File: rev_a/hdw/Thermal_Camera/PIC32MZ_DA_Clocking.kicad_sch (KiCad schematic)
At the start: 17 parts, among them U1101 74LVC1G97, X1101 ASE-8.000MHz, X1102 ECS-327KE

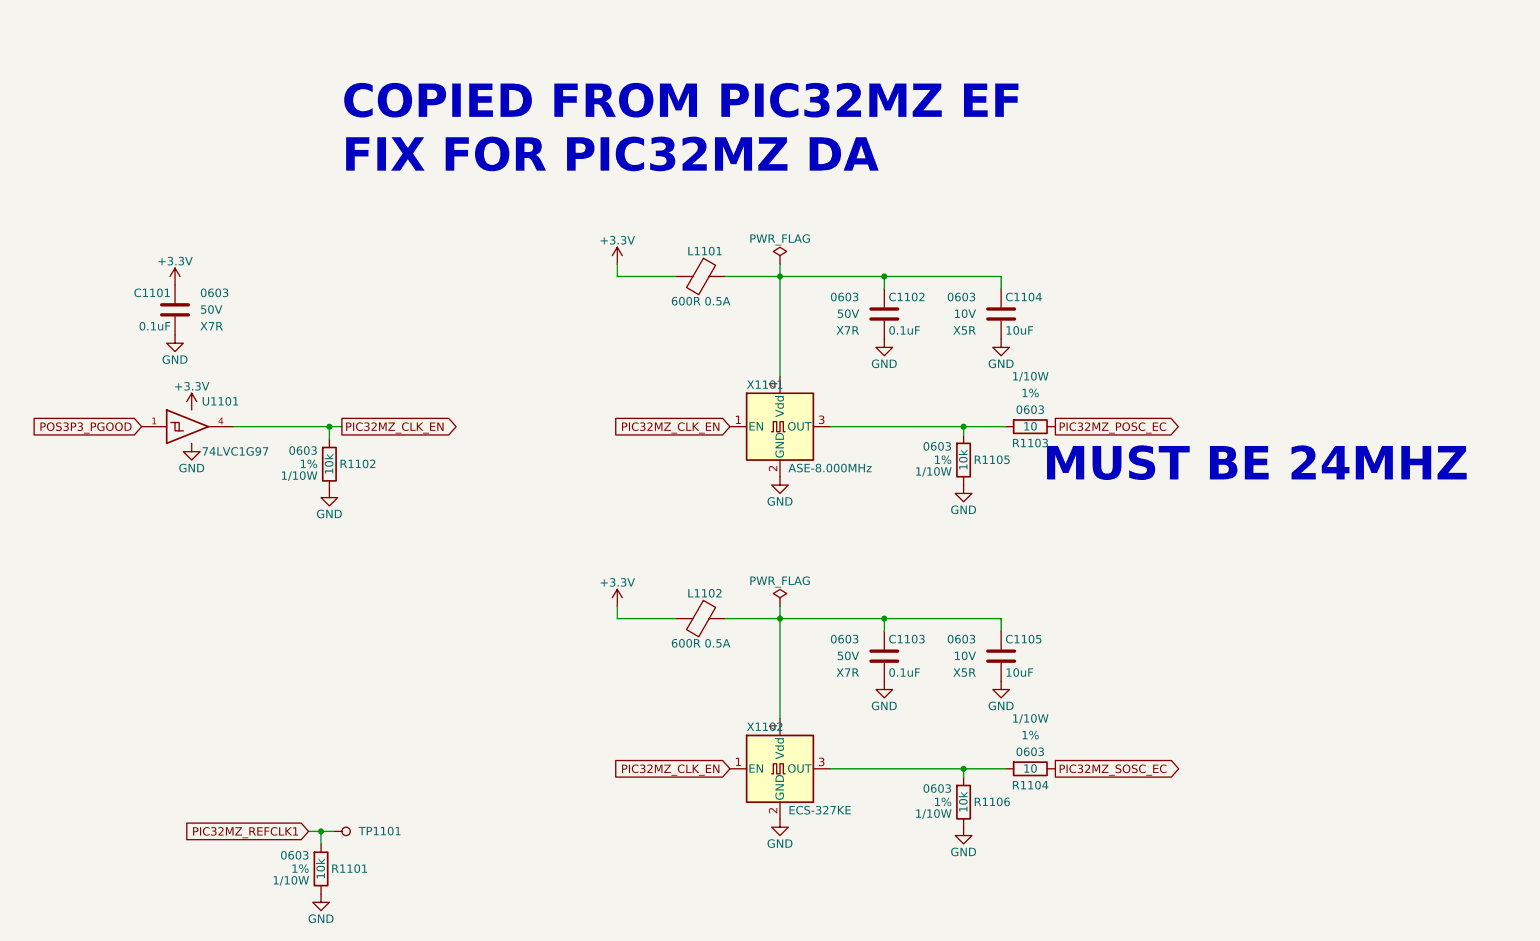
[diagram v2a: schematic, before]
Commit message: changed a lot of circuits from +3.3V to +3.0V VDD
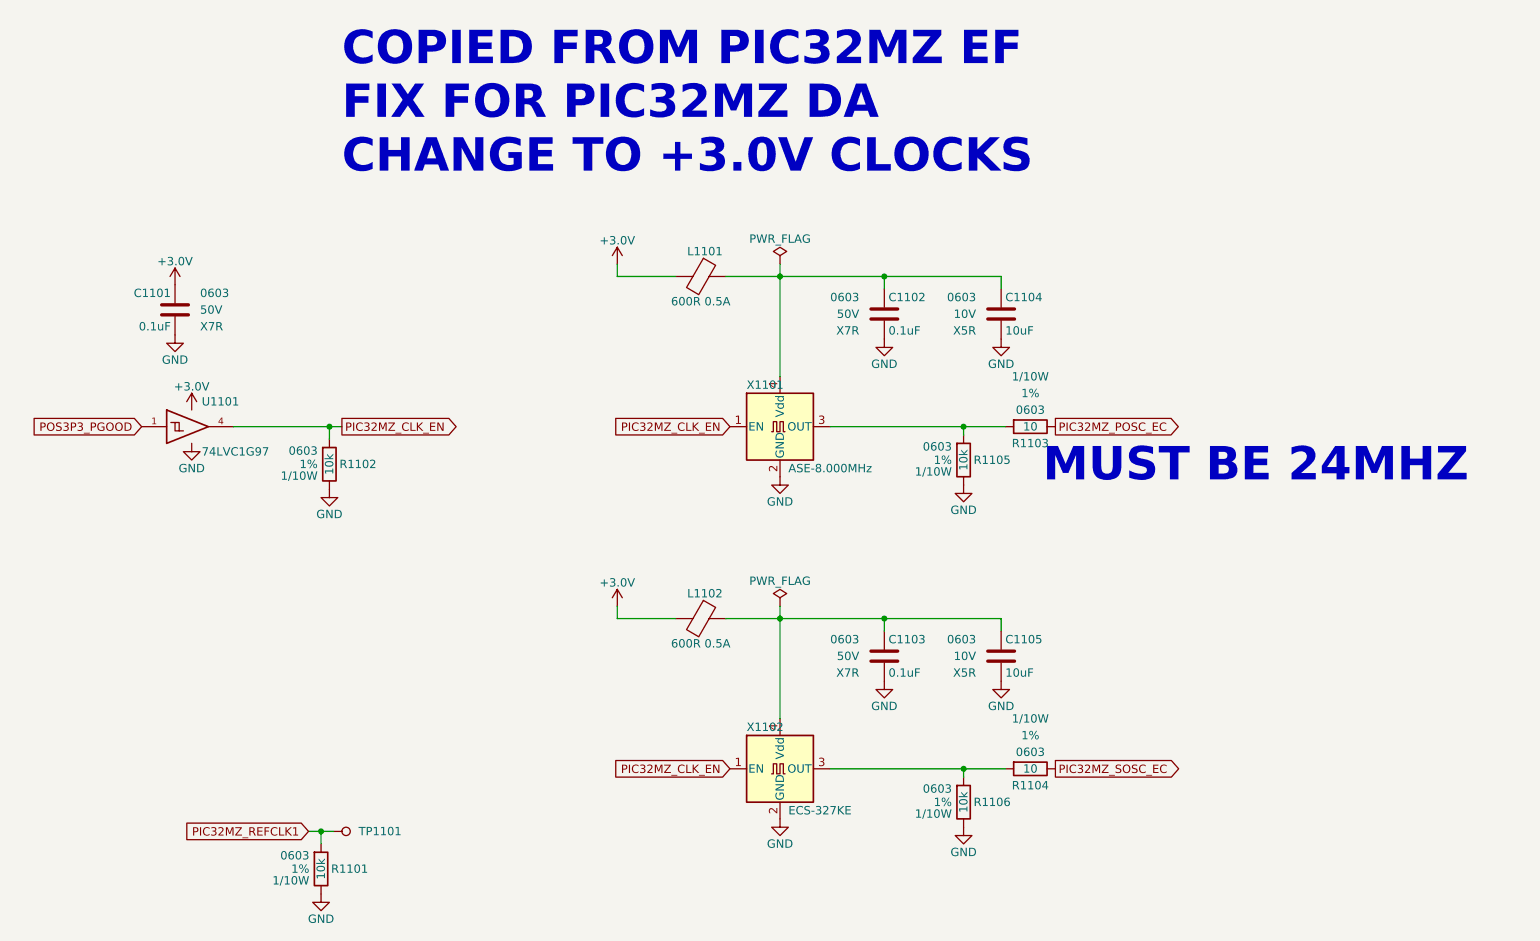
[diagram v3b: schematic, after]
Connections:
- net +3.3V renamed +3.0V
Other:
- note added: "COPIED FROM PIC32MZ EF FIX FOR PIC32MZ DA CHANGE TO +3.0V CLOCKS"
- note removed: "COPIED FROM PIC32MZ EF FIX FOR PIC32MZ DA"
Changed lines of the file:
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@@
     (effects (font (size 5.08 5.08) (thickness 1.016) bold (color 194 0 0 1)) (justify left bottom))
   )
-  (text "COPIED FROM PIC32MZ EF\nFIX FOR PIC32MZ DA" (at 86.36 35.56 0)
+  (text "COPIED FROM PIC32MZ EF\nFIX FOR PIC32MZ DA\nCHANGE TO +3.0V CLOCKS"
+    (at 86.36 35.56 0)
     (effects (font (size 5.08 5.08) (thickness 1.016) bold (color 194 0 0 1)) (justify left bottom))
   )
@@
     )
   )
-  (symbol (lib_id "power:+3.3V") (at 128.27 48.895 0) (unit 1)
-    (in_bom yes) (on_board yes) (dnp no)
-    (property "Reference" "#PWR01107" (at 128.27 52.705 0)
-      (effects (font (size 1.27 1.27)) hide)
-    )
-    (property "Value" "+3.3V" (at 128.27 45.339 0)
-      (effects (font (size 1.27 1.27)))
-    )
-    (property "Footprint" "" (at 128.27 48.895 0)
-      (effects (font (size 1.27 1.27)) hide)
-    )
-    (property "Datasheet" "" (at 128.27 48.895 0)
-      (effects (font (size 1.27 1.27)) hide)
-    )
-    (pin "1")
-    (instances
-      (project "Nixie_Clock_Core"
-        (path "/16fdce21-b570-4d81-a458-e8839d611806/e5c9ef11-2d61-484d-80e2-ac34f2486528"
-          (reference "#PWR01107") (unit 1)
-        )
-      )
-      (project "LED_Panel_Controller"
-        (path "/22e05ee1-b227-4be7-9418-94433f274720/00000000-0000-0000-0000-00005f5829c2"
-          (reference "#PWR?") (unit 1)
-        )
-      )
-      (project "Thermal_Camera"
-        (path "/4bd21e0b-5408-4b93-866e-c82ac5b31fa9/b2bf3717-0f22-469b-940c-2d570066d2c6"
-          (reference "#PWR01007") (unit 1)
-        )
-      )
-    )
-  )
   (symbol (lib_id "Device:Ferrite_Bead") (at 140.97 50.8 270) (unit 1)
     (in_bom yes) (on_board yes) (dnp no)
@@
     )
   )
+  (symbol (lib_id "Custom Library:+3.0V") (at 128.27 100.965 0) (unit 1)
+    (in_bom yes) (on_board yes) (dnp no)
+    (property "Reference" "#PWR01651" (at 128.27 104.775 0)
+      (effects (font (size 1.27 1.27)) hide)
+    )
+    (property "Value" "+3.0V" (at 128.27 97.409 0)
+      (effects (font (size 1.27 1.27)))
+    )
+    (property "Footprint" "" (at 128.27 100.965 0)
+      (effects (font (size 1.27 1.27)) hide)
+    )
+    (property "Datasheet" "" (at 128.27 100.965 0)
+      (effects (font (size 1.27 1.27)) hide)
+    )
+    (pin "1")
+    (instances
+      (project "Thermal_Camera"
+        (path "/4bd21e0b-5408-4b93-866e-c82ac5b31fa9/b2bf3717-0f22-469b-940c-2d570066d2c6"
+          (reference "#PWR01651") (unit 1)
+        )
+      )
+    )
+  )
+  (symbol (lib_id "Custom Library:+3.0V") (at 63.5 71.12 0) (unit 1)
+    (in_bom yes) (on_board yes) (dnp no)
+    (property "Reference" "#PWR01649" (at 63.5 74.93 0)
+      (effects (font (size 1.27 1.27)) hide)
+    )
+    (property "Value" "+3.0V" (at 63.5 67.564 0)
+      (effects (font (size 1.27 1.27)))
+    )
+    (property "Footprint" "" (at 63.5 71.12 0)
+      (effects (font (size 1.27 1.27)) hide)
+    )
+    (property "Datasheet" "" (at 63.5 71.12 0)
+      (effects (font (size 1.27 1.27)) hide)
+    )
+    (pin "1")
+    (instances
+      (project "Thermal_Camera"
+        (path "/4bd21e0b-5408-4b93-866e-c82ac5b31fa9/b2bf3717-0f22-469b-940c-2d570066d2c6"
+          (reference "#PWR01649") (unit 1)
+        )
+      )
+    )
+  )
   (symbol (lib_id "power:GND") (at 168.91 60.325 0) (unit 1)
     (in_bom yes) (on_board yes) (dnp no)
@@
     )
   )
-  (symbol (lib_id "power:+3.3V") (at 60.96 52.07 0) (unit 1)
-    (in_bom yes) (on_board yes) (dnp no)
-    (property "Reference" "#PWR01101" (at 60.96 55.88 0)
-      (effects (font (size 1.27 1.27)) hide)
-    )
-    (property "Value" "+3.3V" (at 60.96 48.514 0)
-      (effects (font (size 1.27 1.27)))
-    )
-    (property "Footprint" "" (at 60.96 52.07 0)
-      (effects (font (size 1.27 1.27)) hide)
-    )
-    (property "Datasheet" "" (at 60.96 52.07 0)
-      (effects (font (size 1.27 1.27)) hide)
-    )
-    (pin "1")
-    (instances
-      (project "Nixie_Clock_Core"
-        (path "/16fdce21-b570-4d81-a458-e8839d611806/e5c9ef11-2d61-484d-80e2-ac34f2486528"
-          (reference "#PWR01101") (unit 1)
-        )
-      )
-      (project "LED_Panel_Controller"
-        (path "/22e05ee1-b227-4be7-9418-94433f274720/00000000-0000-0000-0000-00005f5829c2"
-          (reference "#PWR?") (unit 1)
-        )
-        (path "/22e05ee1-b227-4be7-9418-94433f274720/00000000-0000-0000-0000-00005f582e50"
-          (reference "#PWR?") (unit 1)
-        )
-      )
-      (project "Thermal_Camera"
-        (path "/4bd21e0b-5408-4b93-866e-c82ac5b31fa9/b2bf3717-0f22-469b-940c-2d570066d2c6"
-          (reference "#PWR01001") (unit 1)
+  (symbol (lib_id "Custom Library:+3.0V") (at 128.27 48.895 0) (unit 1)
+    (in_bom yes) (on_board yes) (dnp no)
+    (property "Reference" "#PWR01650" (at 128.27 52.705 0)
+      (effects (font (size 1.27 1.27)) hide)
+    )
+    (property "Value" "+3.0V" (at 128.27 45.339 0)
+      (effects (font (size 1.27 1.27)))
+    )
+    (property "Footprint" "" (at 128.27 48.895 0)
+      (effects (font (size 1.27 1.27)) hide)
+    )
+    (property "Datasheet" "" (at 128.27 48.895 0)
+      (effects (font (size 1.27 1.27)) hide)
+    )
+    (pin "1")
+    (instances
+      (project "Thermal_Camera"
+        (path "/4bd21e0b-5408-4b93-866e-c82ac5b31fa9/b2bf3717-0f22-469b-940c-2d570066d2c6"
+          (reference "#PWR01650") (unit 1)
         )
       )
@@
         (path "/4bd21e0b-5408-4b93-866e-c82ac5b31fa9/b2bf3717-0f22-469b-940c-2d570066d2c6"
           (reference "R?") (unit 1)
-        )
-      )
-    )
-  )
-  (symbol (lib_id "power:+3.3V") (at 128.27 100.965 0) (unit 1)
-    (in_bom yes) (on_board yes) (dnp no)
-    (property "Reference" "#PWR01108" (at 128.27 104.775 0)
-      (effects (font (size 1.27 1.27)) hide)
-    )
-    (property "Value" "+3.3V" (at 128.27 97.409 0)
-      (effects (font (size 1.27 1.27)))
-    )
-    (property "Footprint" "" (at 128.27 100.965 0)
-      (effects (font (size 1.27 1.27)) hide)
-    )
-    (property "Datasheet" "" (at 128.27 100.965 0)
-      (effects (font (size 1.27 1.27)) hide)
-    )
-    (pin "1")
-    (instances
-      (project "Nixie_Clock_Core"
-        (path "/16fdce21-b570-4d81-a458-e8839d611806/e5c9ef11-2d61-484d-80e2-ac34f2486528"
-          (reference "#PWR01108") (unit 1)
-        )
-      )
-      (project "LED_Panel_Controller"
-        (path "/22e05ee1-b227-4be7-9418-94433f274720/00000000-0000-0000-0000-00005f5829c2"
-          (reference "#PWR?") (unit 1)
-        )
-      )
-      (project "Thermal_Camera"
-        (path "/4bd21e0b-5408-4b93-866e-c82ac5b31fa9/b2bf3717-0f22-469b-940c-2d570066d2c6"
-          (reference "#PWR01008") (unit 1)
         )
       )
@@
         (path "/4bd21e0b-5408-4b93-866e-c82ac5b31fa9/b2bf3717-0f22-469b-940c-2d570066d2c6"
           (reference "L?") (unit 1)
+        )
+      )
+    )
+  )
+  (symbol (lib_id "Custom Library:+3.0V") (at 60.96 52.07 0) (unit 1)
+    (in_bom yes) (on_board yes) (dnp no)
+    (property "Reference" "#PWR01648" (at 60.96 55.88 0)
+      (effects (font (size 1.27 1.27)) hide)
+    )
+    (property "Value" "+3.0V" (at 60.96 48.514 0)
+      (effects (font (size 1.27 1.27)))
+    )
+    (property "Footprint" "" (at 60.96 52.07 0)
+      (effects (font (size 1.27 1.27)) hide)
+    )
+    (property "Datasheet" "" (at 60.96 52.07 0)
+      (effects (font (size 1.27 1.27)) hide)
+    )
+    (pin "1")
+    (instances
+      (project "Thermal_Camera"
+        (path "/4bd21e0b-5408-4b93-866e-c82ac5b31fa9/b2bf3717-0f22-469b-940c-2d570066d2c6"
+          (reference "#PWR01648") (unit 1)
         )
       )
@@
         )
       )
-    )
-  )
-  (symbol (lib_id "power:+3.3V") (at 63.5 71.12 0) (unit 1)
-    (in_bom yes) (on_board yes) (dnp no)
-    (property "Reference" "#PWR01103" (at 63.5 74.93 0)
-      (effects (font (size 1.27 1.27)) hide)
-    )
-    (property "Value" "+3.3V" (at 63.5 67.564 0)
-      (effects (font (size 1.27 1.27)))
-    )
-    (property "Footprint" "" (at 63.5 71.12 0)
-      (effects (font (size 1.27 1.27)) hide)
-    )
-    (property "Datasheet" "" (at 63.5 71.12 0)
-      (effects (font (size 1.27 1.27)) hide)
-    )
-    (pin "1")
-    (instances
-      (project "Nixie_Clock_Core"
-        (path "/16fdce21-b570-4d81-a458-e8839d611806/e5c9ef11-2d61-484d-80e2-ac34f2486528"
-          (reference "#PWR01103") (unit 1)
-        )
-      )
-      (project "LED_Panel_Controller"
-        (path "/22e05ee1-b227-4be7-9418-94433f274720/00000000-0000-0000-0000-00005f5829c2"
-          (reference "#PWR?") (unit 1)
-        )
-        (path "/22e05ee1-b227-4be7-9418-94433f274720/00000000-0000-0000-0000-00005f582e50"
-          (reference "#PWR?") (unit 1)
-        )
-      )
-      (project "Thermal_Camera"
-        (path "/4bd21e0b-5408-4b93-866e-c82ac5b31fa9/b2bf3717-0f22-469b-940c-2d570066d2c6"
-          (reference "#PWR01003") (unit 1)
-        )
-      )

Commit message: added PIC32 bypass, SD card load switch, other random junk
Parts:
- removed X1101: ASE-8.000MHz, Oscillator:Oscillator_SMD_Abracon_ASE-4Pin_3.2x2.5mm, symbol Oscillator:ASE-xxxMHz
- added X?: ECS-2520MV-240-BN, Oscillator:Oscillator_SMD_ECS_2520MV-xxx-xx-4Pin_2.5x2.0mm, symbol Oscillator:ECS-2520MV-xxx-xx
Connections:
- net GND: now also X?.2 (GND)
- net PIC32MZ_CLK_EN: now also X?.1 (Tri-State)
- net at R1103.1, R1105.1: now also X?.3 (OUT)
- net at C1102.1, C1104.1, L1101.1: now also X?.4 (VDD)
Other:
- note added: "COPIED FROM PIC32MZ EF FIX FOR PIC32MZ DA"
- note removed: "COPIED FROM PIC32MZ EF FIX FOR PIC32MZ DA CHANGE TO +3.0V CLOCKS"
- note removed: "MUST BE 24MHZ"
- moved on the sheet: C1102, C1103, C1104, C1105, R1101, R1102, R1103, R1104, R1105, R1106, TP1101, X1102

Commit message: added some more USB stuff
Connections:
- net POS3P3_PGOOD renamed POS3P0_PGOOD
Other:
- note removed: "COPIED FROM PIC32MZ EF FIX FOR PIC32MZ DA"
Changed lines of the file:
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@@
     (stroke (width 0) (type default))
-  )
-  (text "COPIED FROM PIC32MZ EF\nFIX FOR PIC32MZ DA" (at 86.36 35.56 0)
-    (effects (font (size 5.08 5.08) (thickness 1.016) bold (color 194 0 0 1)) (justify left bottom))
   )
   (global_label "PIC32MZ_SOSC_EC" (shape output) (at 195.58 125.73 0) (fields_autoplaced)
@@
     )
   )
-  (global_label "POS3P3_PGOOD" (shape input) (at 55.88 73.66 180) (fields_autoplaced)
+  (global_label "POS3P0_PGOOD" (shape input) (at 55.88 73.66 180) (fields_autoplaced)
     (effects (font (size 1.27 1.27)) (justify right))
     (property "Intersheetrefs" "${INTERSHEET_REFS}" (at 38.0366 73.66 0)

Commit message: lots of schematic progress
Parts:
- C?: renamed from C1103; footprint Capacitors_SMD:C_0603 -> (none); Digi-Key PN 1276-1935-1-ND -> (none); display_footprint 0603 -> (none)
- C?: renamed from C1104; footprint Capacitors_SMD:C_0603 -> (none); Digi-Key PN 1276-1871-1-ND -> (none); display_footprint 0603 -> (none)
- C?: renamed from C1102; footprint Capacitors_SMD:C_0603 -> (none); Digi-Key PN 1276-1935-1-ND -> (none); display_footprint 0603 -> (none)
- C?: renamed from C1101; footprint Capacitors_SMD:C_0603 -> (none); Digi-Key PN 1276-1935-1-ND -> (none); display_footprint 0603 -> (none)
- C?: renamed from C1105; footprint Capacitors_SMD:C_0603 -> (none); Digi-Key PN 1276-1871-1-ND -> (none); display_footprint 0603 -> (none)
- L?: renamed from L1101; footprint Inductors_SMD:L_0603 -> (none); Digi-Key PN 490-1014-1-ND -> (none)
- L?: renamed from L1102; footprint Inductors_SMD:L_0603 -> (none); Digi-Key PN 490-1014-1-ND -> (none)
- R?: renamed from R1105; footprint Resistors_SMD:R_0603 -> (none); Digi-Key PN 541-10.0KHCT-ND -> (none); Wattage 1/10W -> (none); display_footprint 0603 -> (none)
- R?: renamed from R1104; footprint Resistors_SMD:R_0603 -> (none); Digi-Key PN 541-10.0HCT-ND -> (none); Wattage 1/10W -> (none); display_footprint 0603 -> (none)
- R?: renamed from R1103; footprint Resistors_SMD:R_0603 -> (none); Digi-Key PN 541-10.0HCT-ND -> (none); Wattage 1/10W -> (none); display_footprint 0603 -> (none)
- R?: renamed from R1101; footprint Resistors_SMD:R_0603 -> (none); Digi-Key PN 541-10.0KHCT-ND -> (none); Wattage 1/10W -> (none); display_footprint 0603 -> (none)
- R?: renamed from R1102; footprint Resistors_SMD:R_0603 -> (none); Digi-Key PN 541-10.0KHCT-ND -> (none); Wattage 1/10W -> (none); display_footprint 0603 -> (none)
- R?: renamed from R1106; footprint Resistors_SMD:R_0603 -> (none); Digi-Key PN 541-10.0KHCT-ND -> (none); Wattage 1/10W -> (none); display_footprint 0603 -> (none)
- gave numbers to parts that had none: 1
- renumbered TP1101 to TP?, U1101 to U?, X1102 to X?
